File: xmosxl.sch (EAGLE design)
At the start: 123 parts, among them IC1 74LVC1T45W6-7, IC2 74LVC1T45W6-7, IC3 74LVC1T45W6-7, IC4 74LVC1T45W6-7, IC5 74LVC1T45W6-7, IC6 74ALVC164245DGG_11, IC7 74ALVC164245DGG_11, IC8 74LVC1T45W6-7, IC9 74LVC1T45W6-7, U1 24 MHz Osc. (F535L-24)

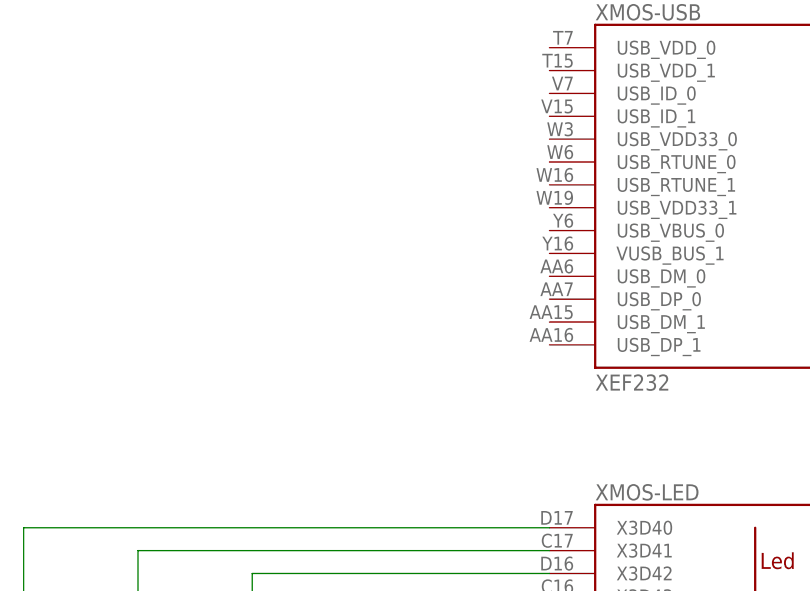
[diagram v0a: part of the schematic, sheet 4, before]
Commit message: Add the USB RTUNE resistors - per XMOS, no more other connections need to be made to the USB ports.
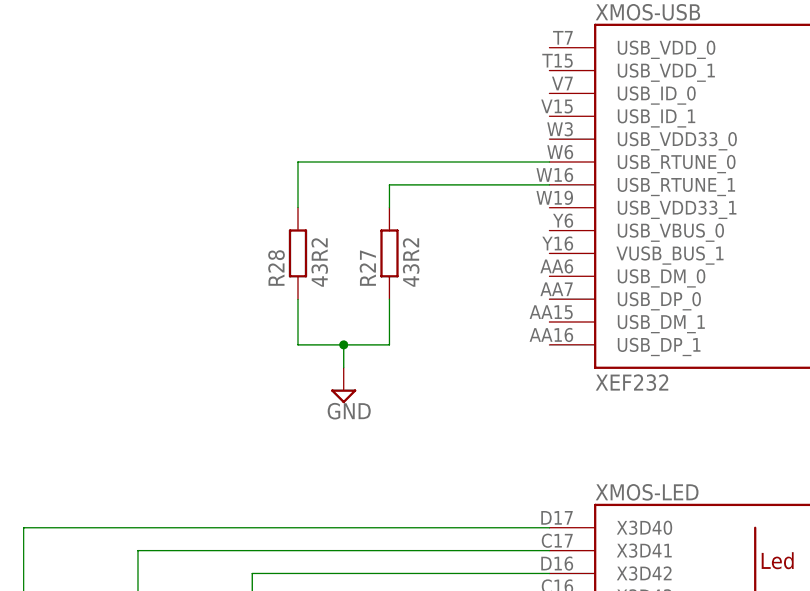
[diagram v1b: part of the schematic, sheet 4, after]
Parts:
- added R27, R28: 43R2, rcl:R-EU_R0201
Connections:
- new net N$11: R27.2, XMOS-USB.USB_RTUNE_1@W16
- new net N$12: R28.2, XMOS-USB.USB_RTUNE_0@W6
- net GND: now also R27.1, R28.1
